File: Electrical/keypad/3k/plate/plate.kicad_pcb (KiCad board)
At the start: 2 copper layers, 68 x 68 mm, 8 parts

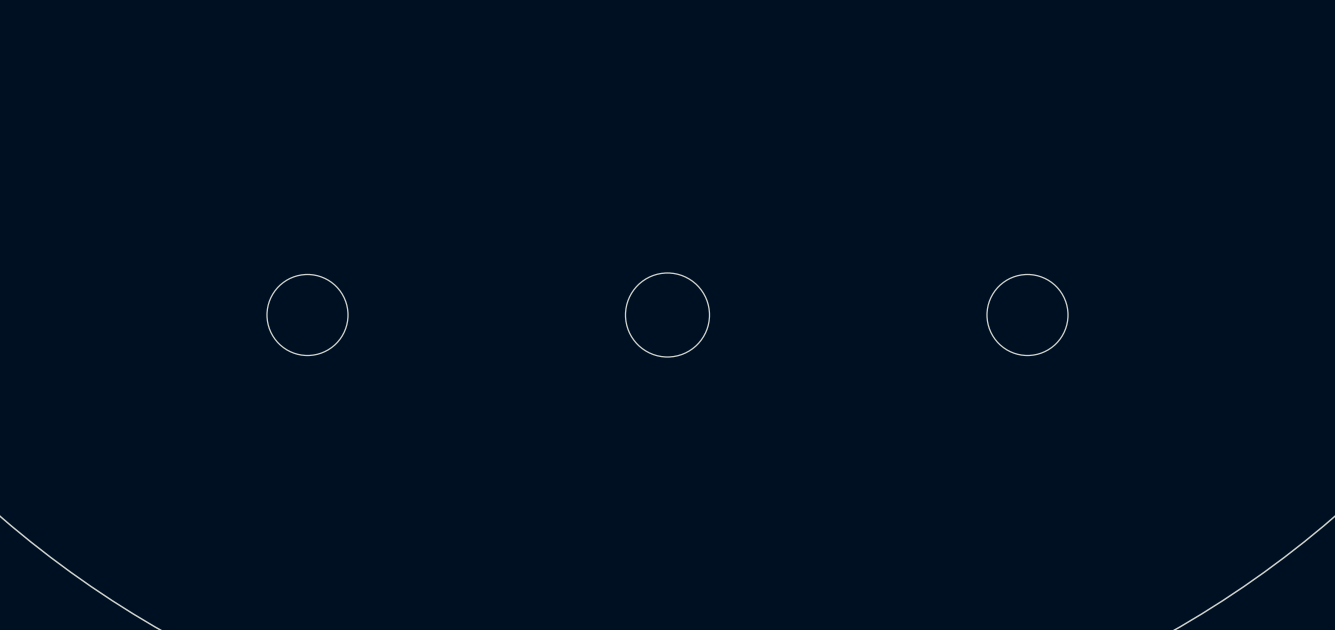
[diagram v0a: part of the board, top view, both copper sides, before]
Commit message: adds instructions to readme, adds the button changes to plate
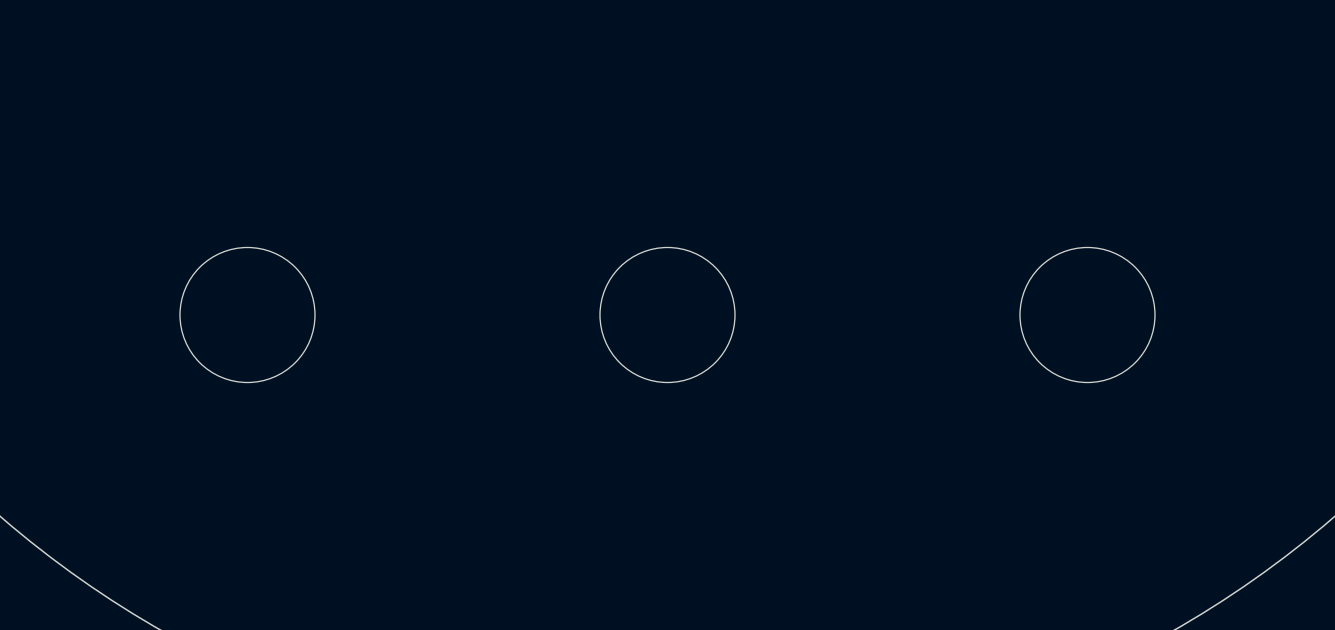
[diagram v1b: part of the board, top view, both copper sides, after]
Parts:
- removed the REF** at (88.0, 119.0)
- removed the REF** at (100.0, 119.0)
- added REF**: MountingHole_4.5mm, MountingHole:MountingHole_4.5mm, F.Cu at (100.0, 119.0)
- added REF**: MountingHole_4.5mm, MountingHole:MountingHole_4.5mm, F.Cu at (86.0, 119.0)
- REF**: value MountingHole_2.7mm -> MountingHole_4.5mm; footprint MountingHole:MountingHole_2.7mm -> MountingHole:MountingHole_4.5mm
- moved REF** 2.00 mm to (114.0, 119.0)
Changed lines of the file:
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@@
       (stroke (width 0.12) (type default)) (fill none) (layer "Edge.Cuts"))
   )
-  (footprint "MountingHole:MountingHole_2.7mm" (layer "F.Cu")
-    (at 88 119)
-    (descr "Mounting Hole 2.7mm, no annular")
-    (tags "mounting hole 2.7mm no annular")
+  (footprint "MountingHole:MountingHole_4.5mm" (layer "F.Cu")
+    (at 100 119)
+    (descr "Mounting Hole 4.5mm, no annular")
+    (tags "mounting hole 4.5mm no annular")
     (attr exclude_from_pos_files exclude_from_bom)
-    (fp_text reference "REF**" (at 0 -3.7) (layer "F.SilkS") hide
-        (effects (font (size 1 1) (thickness 0.15)))
-    )
-    (fp_text value "MountingHole_2.7mm" (at 0 3.7) (layer "F.Fab")
+    (fp_text reference "REF**" (at 0 -5.5) (layer "F.SilkS") hide
+        (effects (font (size 1 1) (thickness 0.15)))
+    )
+    (fp_text value "MountingHole_4.5mm" (at 0 5.5) (layer "F.Fab")
         (effects (font (size 1 1) (thickness 0.15)))
     )
@@
         (effects (font (size 1 1) (thickness 0.15)))
     )
-    (fp_circle (center 0 0) (end 2.7 0)
+    (fp_circle (center 0 0) (end 4.5 0)
       (stroke (width 0.15) (type solid)) (fill none) (layer "Cmts.User"))
-    (fp_circle (center 0 0) (end 2.95 0)
+    (fp_circle (center 0 0) (end 4.75 0)
       (stroke (width 0.05) (type solid)) (fill none) (layer "F.CrtYd"))
-    (pad "" np_thru_hole circle (at 0 0) (size 2.7 2.7) (drill 2.7) (layers "*.Cu" "*.Mask"))
-  )
-  (footprint "MountingHole:MountingHole_2.7mm" (layer "F.Cu")
-    (at 112 119)
-    (descr "Mounting Hole 2.7mm, no annular")
-    (tags "mounting hole 2.7mm no annular")
+    (pad "" np_thru_hole circle (at 0 0) (size 4.5 4.5) (drill 4.5) (layers "F&B.Cu" "*.Mask"))
+  )
+  (footprint "MountingHole:MountingHole_4.5mm" (layer "F.Cu")
+    (at 114 119)
+    (descr "Mounting Hole 4.5mm, no annular")
+    (tags "mounting hole 4.5mm no annular")
     (attr exclude_from_pos_files exclude_from_bom)
-    (fp_text reference "REF**" (at 0 -3.7) (layer "F.SilkS") hide
-        (effects (font (size 1 1) (thickness 0.15)))
-    )
-    (fp_text value "MountingHole_2.7mm" (at 0 3.7) (layer "F.Fab")
+    (fp_text reference "REF**" (at 0 -5.5) (layer "F.SilkS") hide
+        (effects (font (size 1 1) (thickness 0.15)))
+    )
+    (fp_text value "MountingHole_4.5mm" (at 0 5.5) (layer "F.Fab")
         (effects (font (size 1 1) (thickness 0.15)))
     )
@@
         (effects (font (size 1 1) (thickness 0.15)))
     )
-    (fp_circle (center 0 0) (end 2.7 0)
+    (fp_circle (center 0 0) (end 4.5 0)
       (stroke (width 0.15) (type solid)) (fill none) (layer "Cmts.User"))
-    (fp_circle (center 0 0) (end 2.95 0)
+    (fp_circle (center 0 0) (end 4.75 0)
       (stroke (width 0.05) (type solid)) (fill none) (layer "F.CrtYd"))
-    (pad "" np_thru_hole circle (at 0 0) (size 2.7 2.7) (drill 2.7) (layers "*.Cu" "*.Mask"))
+    (pad "" np_thru_hole circle (at 0 0) (size 4.5 4.5) (drill 4.5) (layers "*.Cu" "*.Mask"))
   )
   (footprint "MountingHole:MountingHole_2.7mm_M2.5" (layer "F.Cu")
@@
     (pad "" np_thru_hole circle (at 0 0) (size 2.7 2.7) (drill 2.7) (layers "F&B.Cu" "*.Mask"))
   )
+  (footprint "MountingHole:MountingHole_4.5mm" (layer "F.Cu")
+    (at 86 119)
+    (descr "Mounting Hole 4.5mm, no annular")
+    (tags "mounting hole 4.5mm no annular")
+    (attr exclude_from_pos_files exclude_from_bom)
+    (fp_text reference "REF**" (at 0 -5.5) (layer "F.SilkS") hide
+        (effects (font (size 1 1) (thickness 0.15)))
+    )
+    (fp_text value "MountingHole_4.5mm" (at 0 5.5) (layer "F.Fab")
+        (effects (font (size 1 1) (thickness 0.15)))
+    )
+    (fp_text user "${REFERENCE}" (at 0 0) (layer "F.Fab")
+        (effects (font (size 1 1) (thickness 0.15)))
+    )
+    (fp_circle (center 0 0) (end 4.5 0)
+      (stroke (width 0.15) (type solid)) (fill none) (layer "Cmts.User"))
+    (fp_circle (center 0 0) (end 4.75 0)
+      (stroke (width 0.05) (type solid)) (fill none) (layer "F.CrtYd"))
+    (pad "" np_thru_hole circle (at 0 0) (size 4.5 4.5) (drill 4.5) (layers "F&B.Cu" "*.Mask"))
+  )
   (footprint "Button_Switch_Keyboard:SW_Lekker_1.00u_Plate" (layer "F.Cu")
     (at 119.05 100)
@@
       (stroke (width 0.12) (type default)) (fill none) (layer "Edge.Cuts"))
   )
-  (footprint "MountingHole:MountingHole_2.7mm" (layer "F.Cu")
-    (at 100 119)
-    (descr "Mounting Hole 2.7mm, no annular")
-    (tags "mounting hole 2.7mm no annular")
-    (attr exclude_from_pos_files exclude_from_bom)
-    (fp_text reference "REF**" (at 0 -3.7) (layer "F.SilkS") hide
-        (effects (font (size 1 1) (thickness 0.15)))
-    )
-    (fp_text value "MountingHole_2.7mm" (at 2.754926 4.63036) (layer "F.Fab")
-        (effects (font (size 1 1) (thickness 0.15)))
-    )
-    (fp_circle (center 0 0) (end 2.7 0)
-      (stroke (width 0.15) (type solid)) (fill none) (layer "Cmts.User"))
-    (fp_circle (center 0 0) (end 2.95 0)
-      (stroke (width 0.05) (type solid)) (fill none) (layer "F.CrtYd"))
-    (pad "" np_thru_hole circle (at 0 0) (size 2.8 2.8) (drill 2.8) (layers "F&B.Cu" "*.Mask"))
-  )
   (gr_circle (center 100 100) (end 134 100)
     (stroke (width 0.05) (type default)) (fill none) (layer "Edge.Cuts"))
@@
   )
   (gr_text "H2" (at 162.032794 51.70701 -180) (layer "B.Fab")
+    (effects (font (size 1 1) (thickness 0.15)) (justify mirror))
+  )
+  (gr_text "H2" (at 87.467794 118.30201 -180) (layer "B.Fab")
     (effects (font (size 1 1) (thickness 0.15)) (justify mirror))
   )
@@
     (polygon
       (pts
-        (xy 78.45 116.9)
-        (xy 76.369159 120.486133)
-        (xy 80.515262 120.495128)
+        (xy 77.508178 116.64314)
+        (xy 75.427337 120.229273)
+        (xy 79.57344 120.238268)
       )
     )
@@
     (polygon
       (pts
+        (xy 79.367794 122.80201)
+        (xy 83.529476 115.629746)
+        (xy 87.66 122.82)
+      )
+    )
+  )
+  (zone (net 0) (net_name "") (layers "F&B.Cu" "F.Mask") (hatch edge 0.5)
+    (connect_pads (clearance 0))
+    (min_thickness 0.25) (filled_areas_thickness no)
+    (keepout (tracks not_allowed) (vias not_allowed) (pads not_allowed) (copperpour not_allowed) (footprints allowed))
+    (fill (thermal_gap 0.5) (thermal_bridge_width 0.5))
+    (polygon
+      (pts
         (xy 243.561691 60.373015)
         (xy 249.804214 49.614618)
@@
         (xy 68.669476 103.409746)
         (xy 72.8 110.6)
-      )
-    )
-  )
-  (zone (net 0) (net_name "") (layers "F&B.Cu" "F.Mask") (hatch edge 0.5)
-    (connect_pads (clearance 0))
-    (min_thickness 0.25) (filled_areas_thickness no)
-    (keepout (tracks not_allowed) (vias not_allowed) (pads not_allowed) (copperpour not_allowed) (footprints allowed))
-    (fill (thermal_gap 0.5) (thermal_bridge_width 0.5))
-    (polygon
-      (pts
-        (xy 81.00851 123.491811)
-        (xy 85.170192 116.319547)
-        (xy 89.300716 123.509801)
       )
     )
@@
     (polygon
       (pts
+        (xy 79.367794 122.80201)
+        (xy 83.529476 115.629746)
+        (xy 87.66 122.82)
+      )
+    )
+  )
+  (zone (net 0) (net_name "") (layers "*.Mask") (hatch edge 0.5)
+    (connect_pads (clearance 0))
+    (min_thickness 0.25) (filled_areas_thickness no)
+    (fill yes (thermal_gap 0.5) (thermal_bridge_width 0.5))
+    (polygon
+      (pts
         (xy 178.225312 34.30166)
         (xy 186.548676 19.957132)
@@
       )
     )
-  )
-  (zone (net 0) (net_name "") (layers "*.Mask") (hatch edge 0.5)
-    (connect_pads (clearance 0))
-    (min_thickness 0.25) (filled_areas_thickness no)
-    (fill yes (thermal_gap 0.5) (thermal_bridge_width 0.5))
-    (polygon
-      (pts
-        (xy 81.00851 123.491811)
-        (xy 85.170192 116.319547)
-        (xy 89.300716 123.509801)
-      )
-    )
